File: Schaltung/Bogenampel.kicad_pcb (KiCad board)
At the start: 2 copper layers, 95 x 62 mm, 32 parts, among them J1 WS2812B Stripe Timer, J10 Display, J2 Conn_01x04_Pin, J3 DC/DC Boost, J4 Jumper: 5V/Ext Voltage, J5 Buzzer, J6 Battery, J7 Input 4, J8 Input 5, J9 Power Bank, Q1 IRLZ44N, U1 NRF24L01_Breakout, U2 TXS0108EPW

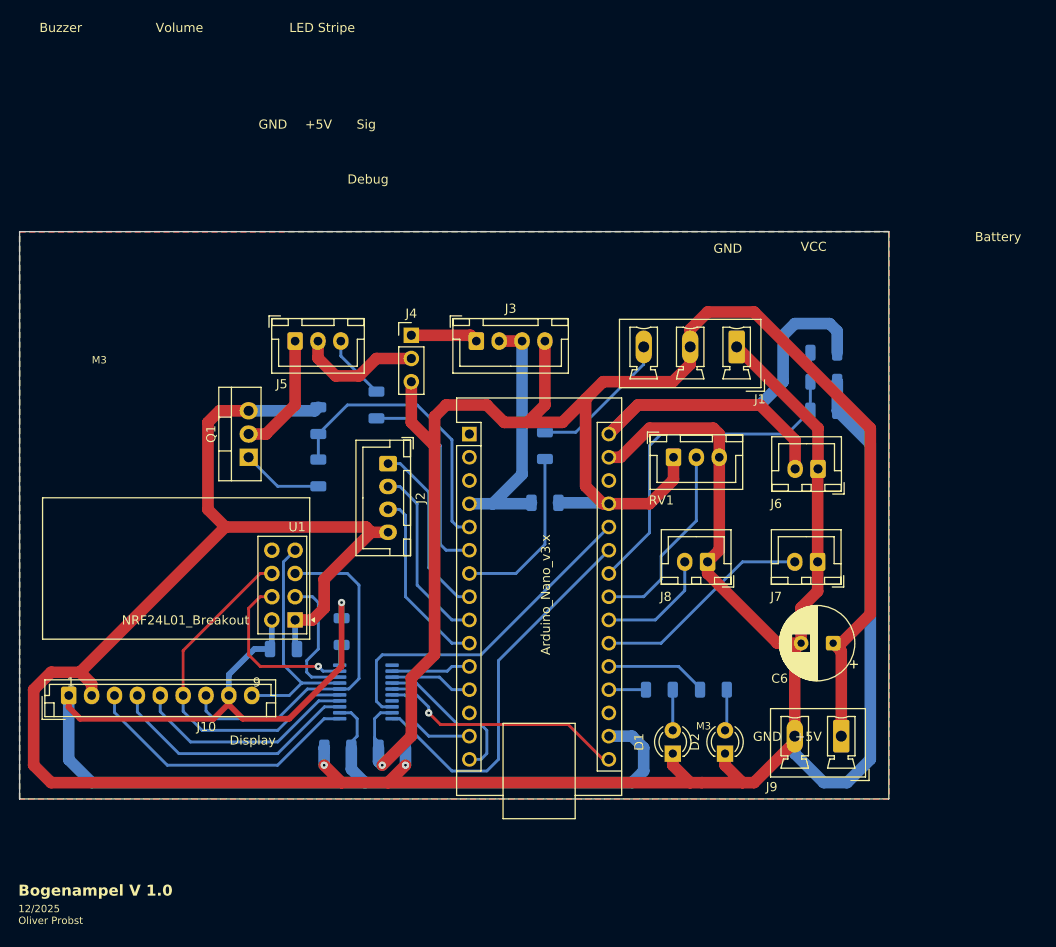
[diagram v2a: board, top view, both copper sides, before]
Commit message: 7-Segment LED-Display und Gruppen-Anzeige implementiert
Empfänger:
- 158 LEDs konfiguriert: 16 Gruppe A/B, 16 Gruppe C/D, 126 für 3×7-Segment Displays
- Timer-Countdown auf 7-Segment-Display (Grün > Orange > Rot)
- Vorbereitungsphase (10s) mit Countdown in ROT
- Orange statt Gelb für letzte 30 Sekunden (besserer Kontrast zu Grün)
- Gruppen-Farbe synchron mit Display-Farbe
- Gruppen-Umschaltung korrigiert (inaktive Gruppe wird ausgeschaltet)
- Buzzer-Funktionen verbessert (explizites Pin-Reset)
- segmentMap korrigiert für korrekte 7-Segment-Darstellung
- Display-Reihenfolge angepasst (1er, 10er, 100er von links nach rechts)

Sender:
- Gruppen-Kommandos jetzt zur richtigen Zeit gesendet (nach advanceToNextGroup)

🤖 Generated with Claude Code

Co-Authored-By: Claude Sonnet 4.5 <noreply@anthropic.com>
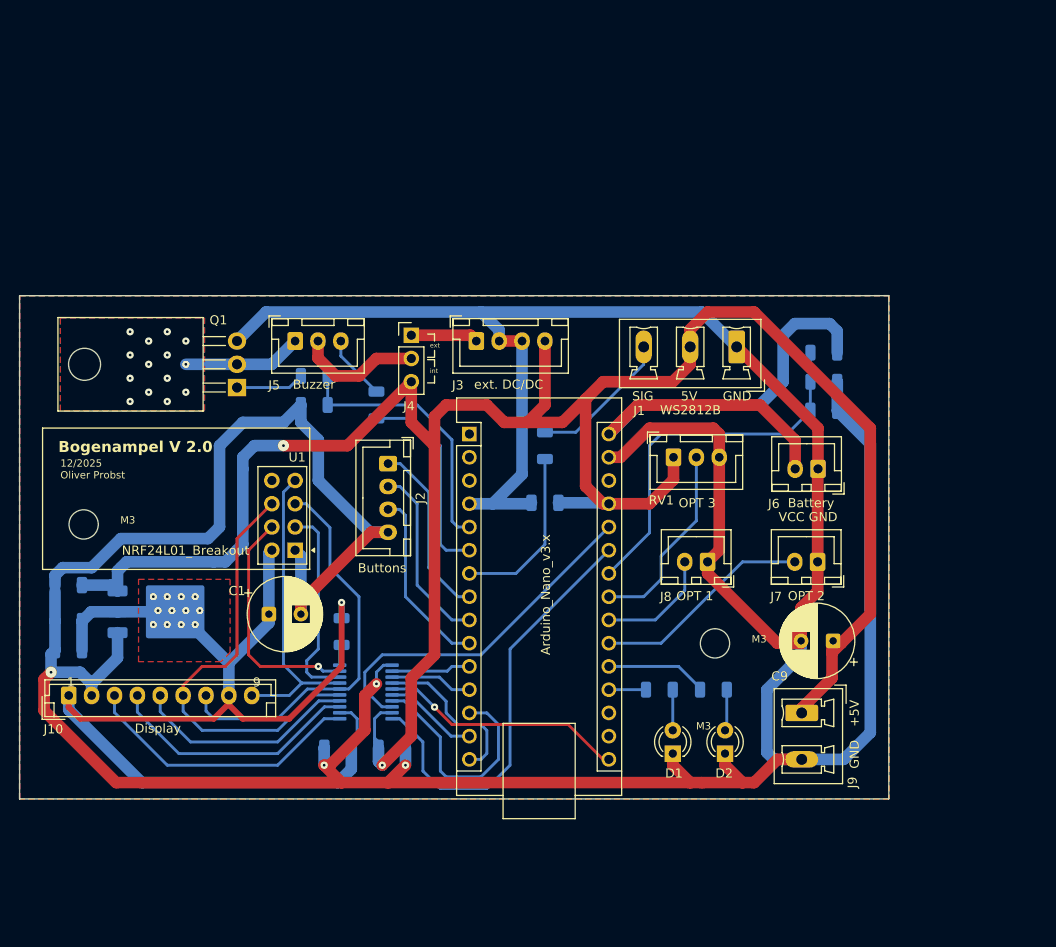
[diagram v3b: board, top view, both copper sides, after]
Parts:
- added C5: 100nF, Capacitor_SMD:C_1206_3216Metric, B.Cu at (93.3, 94.7)
- added C7: 10µF, Capacitor_SMD:C_1206_3216Metric, B.Cu at (93.3, 91.6)
- added C8: 10µF, Capacitor_SMD:C_1206_3216Metric, B.Cu at (93.3, 87.6)
- added REF**: MountingHole_3.2mm_M3, MountingHole:MountingHole_3.2mm_M3, F.Cu at (95.0, 81.0)
- added REF**: MountingHole_3.2mm_M3, MountingHole:MountingHole_3.2mm_M3, F.Cu at (164.0, 94.0)
- added U3: LM1117DT-3.3, Package_TO_SOT_SMD:TO-252-3_TabPin2, B.Cu at (103.7, 90.5)
- C1: value 10µF -> 100µF; footprint Capacitor_SMD:C_1206_3216Metric -> Capacitor_THT:CP_Radial_D8.0mm_P3.50mm; moved to F.Cu
- Q1: footprint Package_TO_SOT_THT:TO-220-3_Vertical -> Package_TO_SOT_THT:TO-220-3_Horizontal_TabDown
- moved R3 10.6 mm to (120.2, 64.8), turned to 180 degrees
- moved Q1 7.73 mm to (111.8, 66.0)
- moved U1 7.62 mm to (118.1, 83.8)
- moved J9 5.01 mm to (173.5, 101.6), turned to -90 degrees
- moved C1 4.13 mm to (115.2, 90.8)
- moved R4 1.77 mm to (120.2, 67.9), turned to 0 degrees
- moved C9 0.25 mm to (176.9, 93.7)
- renumbered C5 to C6, C6 to C9
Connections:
- A1 pad 17: +3.3V -> unconnected-(A1-3V3-Pad17)
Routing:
- net GND: track 377.4 -> 464.4 mm, vias 2 -> 4
- net +5V: track 193.1 -> 245.6 mm, vias 1 -> 2
- net /DSPL_DC_5V: track 0.00 -> 25.5 mm
- net +3.3V: track 145.5 -> 130.0 mm, vias 1 -> 13
- net /SPI_3V3.MOSI: track 39.4 -> 47.8 mm
- net /NRF_CS_3V3: track 14.8 -> 22.4 mm
- net /SPI_3V3.MISO: track 26.0 -> 33.7 mm
- net /NRF_CSN_3V3: track 18.8 -> 25.7 mm
- net /SPI_3V3.SCK: track 38.3 -> 43.3 mm
- net /DSPL_CS_5V: track 42.4 -> 46.9 mm
- net Net-(A1-D2): track 31.3 -> 29.4 mm
- net Net-(Q1-G): track 8.94 -> 7.51 mm
- net /SPI_5V.MOSI: track 11.4 -> 10.3 mm
- net /DSPL_RES_5V: track 37.9 -> 38.9 mm
- net /SPI_5V.MISO: track 17.2 -> 17.9 mm
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- added copper zone on F.Cu, net +3.3V
- added copper zone on B.Cu, net Net-(J5-Pin_1)
- added copper zone on F.Cu, net Net-(J5-Pin_1)
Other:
- board size 95 x 62 mm -> 95 x 55 mm
- board text added: "5V"
- board text added: "Bogenampel V 2.0"
- board text added: "Buttons"
- board text added: "OPT 1"
- board text added: "OPT 2"
- board text added: "OPT 3"
- board text added: "SIG"
- board text added: "WS2812B"
- board text added: "ext"
- board text added: "ext. DC/DC"
- board text added: "int"
- board text removed: "Bogenampel V 1.0"
- board text removed: "Debug"
- board text removed: "LED Stripe"
- board text removed: "Sig"
- board text removed: "Volume"

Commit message: DEBUG_SHORT_TIMES aktiviert mit optimierten Zeiten
Software-Änderungen:
- DEBUG_SHORT_TIMES auf 1 gesetzt (aktiviert)
- Vorbereitungsphase: 5 Sekunden (unverändert)
- Schießzeit: 15 Sekunden für beide Modi (statt 6s/12s)
- Gelbe Ampel: Aktivierung in den letzten 5 Sekunden (statt 30s)
- Empfänger Serial Baud: 115200 statt 57600
- CMD_STOP Handler vereinfacht (nur Vorbereitung zurücksetzen)

Schaltungs-Änderungen:
- MOSFET Q1 Footprint: TO-220-3_Vertical statt Horizontal
- 100nF SMD-Entkopplungskondensator (C10) hinzugefügt
- Spannungsversorgung verbessert

🤖 Generated with [Claude Code](https://claude.com/claude-code)

Co-Authored-By: Claude Sonnet 4.5 <noreply@anthropic.com>
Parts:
- added C10: 100nF, Capacitor_SMD:C_1206_3216Metric, B.Cu at (116.9, 87.4)
- Q1: footprint Package_TO_SOT_THT:TO-220-3_Horizontal_TabDown -> Package_TO_SOT_THT:TO-220-3_Vertical

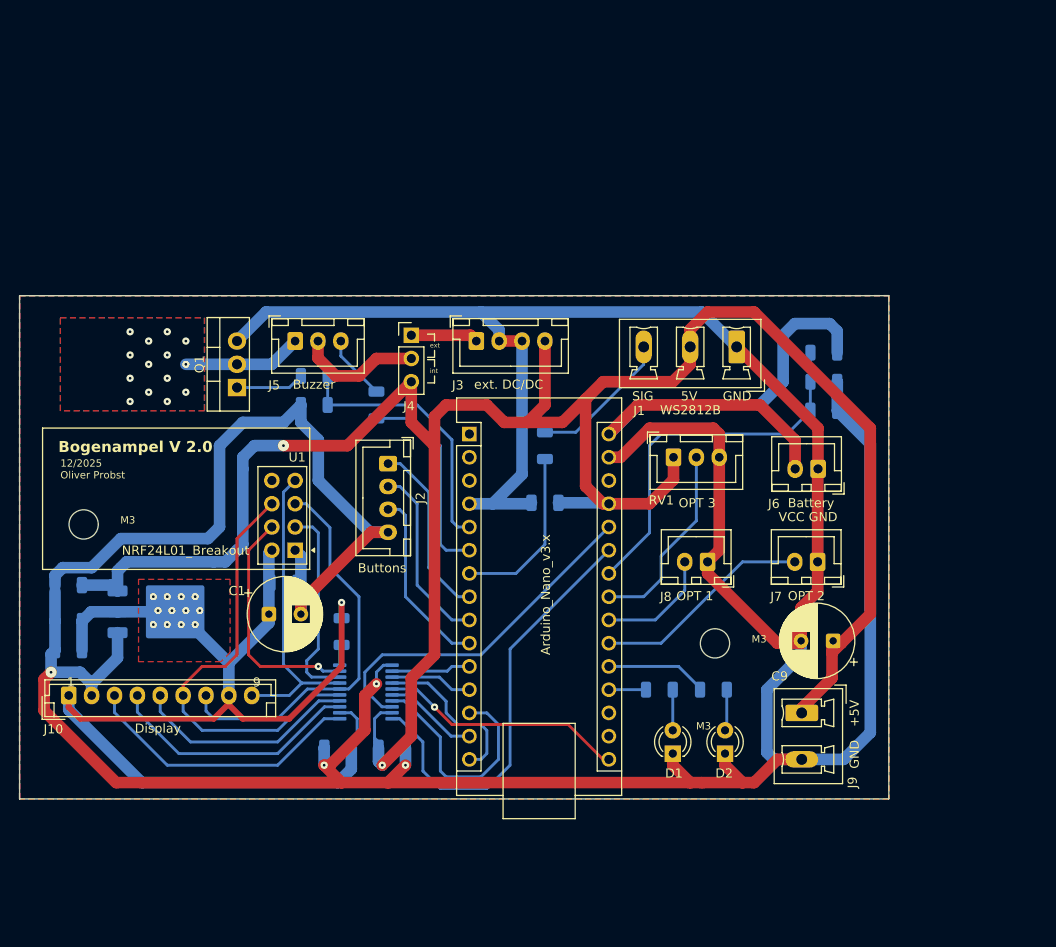
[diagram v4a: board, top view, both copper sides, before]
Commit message: Dokumentation aktualisiert und Schaltung Version 2.2
- HARDWARE.md: Pin-Belegungen korrigiert (NRF D9/D8, Buttons D5/D6/D7, Voltage A5, Buzzer D4)
- README.md: Features, Pin-Tabellen und Kommunikation aktualisiert (158 LEDs, 11 Kommandos)
- Sender/README.md: Alle Features als implementiert markiert, State Machine erweitert
- Sender/SETUP.md: Test-Sektion aktualisiert
- CLAUDE.md: Komplett überarbeitet mit aktuellem Projekt-Stand
- Schaltung: Version 2.2 - bereit für Fertigung
- Test-Dateien entfernt (TestEmpfaenger, TestSender)

🤖 Generated with [Claude Code](https://claude.com/claude-code)

Co-Authored-By: Claude Sonnet 4.5 <noreply@anthropic.com>
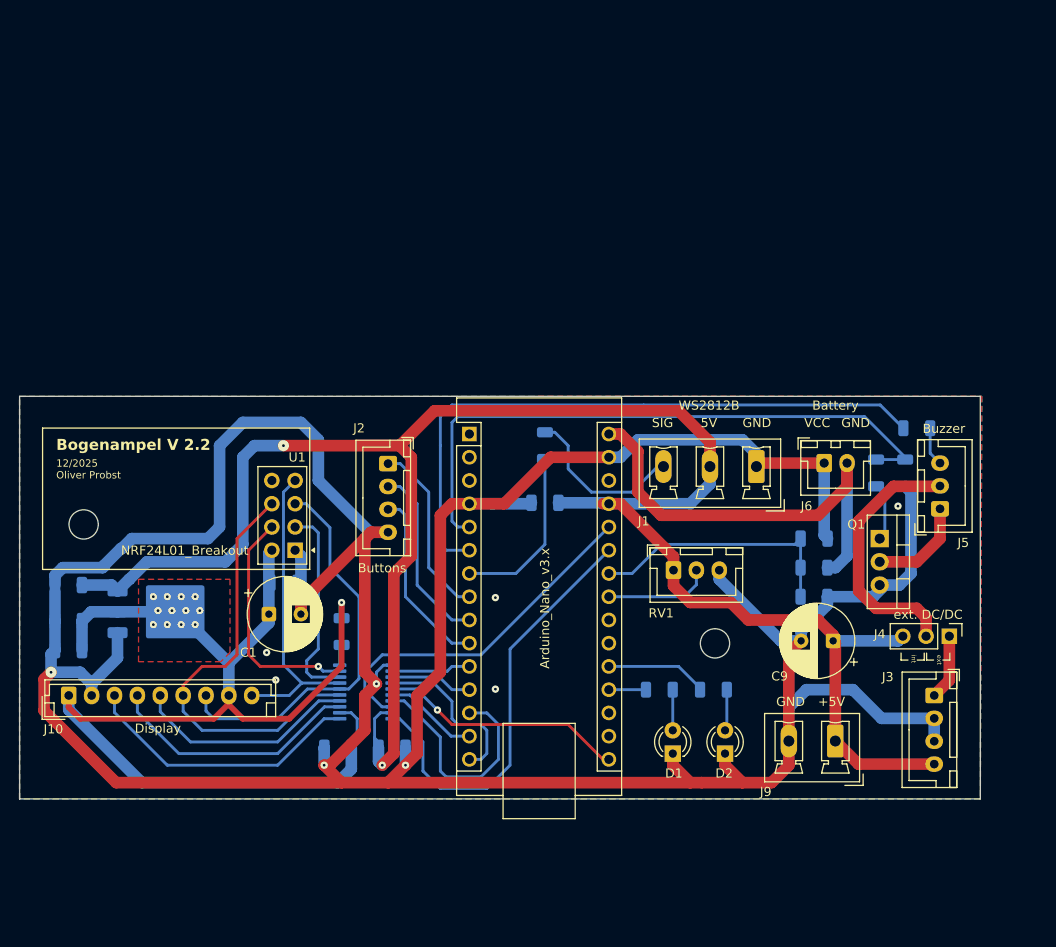
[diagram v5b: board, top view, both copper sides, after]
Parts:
- removed J7: Input 4, Connector_JST:JST_XH_B2B-XH-A_1x02_P2.50mm_Vertical
- removed J8: Input 5, Connector_JST:JST_XH_B2B-XH-A_1x02_P2.50mm_Vertical
- moved J5 72.8 mm to (188.6, 79.3), turned to 90 degrees
- moved Q1 72.2 mm to (182.0, 82.5), turned to -90 degrees
- moved J4 67.4 mm to (189.6, 93.2), turned to -90 degrees
- moved R4 65.0 mm to (184.8, 75.4), turned to 90 degrees
- moved J3 63.3 mm to (188.0, 99.7), turned to -90 degrees
- moved R3 62.3 mm to (181.6, 75.4), turned to -90 degrees
- moved R2 59.1 mm to (186.1, 70.5), turned to 0 degrees
- moved R8 23.5 mm to (174.8, 88.9)
- moved R7 23.5 mm to (174.8, 85.7)
- moved C3 14.0 mm to (174.8, 82.5)
- moved J1 13.3 mm to (168.5, 74.7)
- moved RV1 12.3 mm to (159.5, 86.0)
- moved J9 4.79 mm to (177.2, 104.7), turned to 180 degrees
- moved J6 0.93 mm to (175.9, 74.3), turned to 0 degrees
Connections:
- A1 pad 21: /DI4 -> unconnected-(A1-A2-Pad21)
- A1 pad 22: /DI5 -> unconnected-(A1-A3-Pad22)
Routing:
- net GND: track 464.4 -> 408.5 mm, vias 4 -> 9
- net Net-(A1-D3): track 22.5 -> 69.6 mm
- net Net-(A1-D2): track 29.4 -> 68.0 mm
- net +5V: track 245.6 -> 215.4 mm
- net /DI4: track 24.0 -> 0.00 mm
- net Net-(J4-Pin_2): track 13.7 -> 28.8 mm
- net +BATT: track 62.0 -> 49.0 mm
- net /DI5: track 12.8 -> 0.00 mm
- net /BAT_MON: track 41.3 -> 28.9 mm
- net /AI1: track 21.4 -> 11.7 mm
- net Net-(J5-Pin_3): track 7.13 -> 4.26 mm
- net Net-(J5-Pin_1): track 13.0 -> 10.2 mm, vias 14 -> 0
- net Net-(J1-Pin_3): track 15.8 -> 18.3 mm
- net Net-(Q1-G): track 7.51 -> 6.11 mm
- removed copper zone on B.Cu, net (none)
- removed copper zone on F.Cu, net (none)
- removed copper zone on B.Cu, net Net-(J5-Pin_1)
- removed copper zone on F.Cu, net Net-(J5-Pin_1)
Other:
- board size 95 x 55 mm -> 105 x 44 mm
- board text added: "Bogenampel V 2.2"
- board text removed: "1"
- board text removed: "9"
- board text removed: "Bogenampel V 2.0"
- board text removed: "M3"
- board text removed: "OPT 1"
- board text removed: "OPT 2"
- board text removed: "OPT 3"

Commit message: Bug: A6 & A7 durch A2 & A3 ersetzt für Digital Output
Co-Authored-By: Claude Opus 4.5 <noreply@anthropic.com>
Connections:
- A1 pad 21: unconnected-(A1-A2-Pad21) -> /DSPL_CS_5V
- A1 pad 22: unconnected-(A1-A3-Pad22) -> /DSPL_RES_5V
- A1 pad 25: /DSPL_CS_5V -> unconnected-(A1-A6-Pad25)
- A1 pad 26: /DSPL_RES_5V -> unconnected-(A1-A7-Pad26)
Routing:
- net /DSPL_CS_5V: track 46.9 -> 38.7 mm
- net /DSPL_RES_5V: track 38.9 -> 34.7 mm
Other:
- board text added: "01/2026 Oliver Probst"
- board text added: "Bogenampel V 2.3"
- board text removed: "12/2025 Oliver Probst"
- board text removed: "Bogenampel V 2.2"
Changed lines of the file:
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@@
 	(net 45 "Net-(J5-Pin_1)")
 	(net 46 "unconnected-(A1-3V3-Pad17)")
-	(net 47 "unconnected-(A1-A2-Pad21)")
-	(net 48 "unconnected-(A1-A3-Pad22)")
+	(net 47 "unconnected-(A1-A7-Pad26)")
+	(net 48 "unconnected-(A1-A6-Pad25)")
 	(footprint "LED_THT:LED_D3.0mm"
 		(layer "F.Cu")
@@
 			(layers "*.Cu" "*.Mask")
 			(remove_unused_layers no)
-			(net 47 "unconnected-(A1-A2-Pad21)")
+			(net 21 "/DSPL_CS_5V")
 			(pinfunction "A2")
 			(pintype "bidirectional")
@@
 			(layers "*.Cu" "*.Mask")
 			(remove_unused_layers no)
-			(net 48 "unconnected-(A1-A3-Pad22)")
+			(net 6 "/DSPL_RES_5V")
 			(pinfunction "A3")
 			(pintype "bidirectional")
@@
 			(layers "*.Cu" "*.Mask")
 			(remove_unused_layers no)
-			(net 21 "/DSPL_CS_5V")
+			(net 48 "unconnected-(A1-A6-Pad25)")
 			(pinfunction "A6")
 			(pintype "bidirectional")
@@
 			(layers "*.Cu" "*.Mask")
 			(remove_unused_layers no)
-			(net 6 "/DSPL_RES_5V")
+			(net 47 "unconnected-(A1-A7-Pad26)")
 			(pinfunction "A7")
 			(pintype "bidirectional")
@@
 			)
 		)
-		(property "Datasheet" ""
+		(property "Datasheet" "http://www.irf.com/product-info/datasheets/data/irlz44n.pdf"
 			(at 0 0 90)
 			(layer "F.Fab")
@@
 			)
 		)
-		(property "Description" ""
+		(property "Description" "47A Id, 55V Vds, 22mOhm Rds Single N-Channel HEXFET Power MOSFET, TO-220AB"
 			(at 0 0 90)
 			(layer "F.Fab")
@@
 		)
 	)
-	(gr_text "Bogenampel V 2.2"
+	(gr_text "Bogenampel V 2.3"
 		(at 92 73 0)
 		(layer "F.SilkS")
@@
 		)
 	)
-	(gr_text "12/2025\nOliver Probst"
+	(gr_text "01/2026\nOliver Probst"
 		(at 92 76.073 0)
 		(layer "F.SilkS")
@@
 		)
 	)
-	(gr_text "12/2025\nOliver Probst"
+	(gr_text "01/2026\nOliver Probst"
 		(at 109 76.073 0)
 		(layer "B.SilkS")
@@
 		)
 	)
-	(gr_text "Bogenampel V 2.2"
-		(at 109 73.025 0)
+	(gr_text "Bogenampel V 2.3"
+		(at 109 73 0)
 		(layer "B.SilkS")
 		(effects
@@
 	)
 	(segment
+		(start 143.75 95.25)
+		(end 147.56 91.44)
+		(width 0.318)
+		(layer "B.Cu")
+		(net 6)
+	)
+	(segment
 		(start 125.73 97.155)
 		(end 127.635 95.25)
@@
 	)
 	(segment
+		(start 147.56 91.44)
+		(end 152.4 91.44)
+		(width 0.318)
+		(layer "B.Cu")
+		(net 6)
+	)
+	(segment
+		(start 138.43 95.25)
+		(end 143.75 95.25)
+		(width 0.318)
+		(layer "B.Cu")
+		(net 6)
+	)
+	(segment
 		(start 128.71 100.935)
 		(end 127.605 100.935)
@@
 	)
 	(segment
-		(start 138.43 95.25)
-		(end 152.4 81.28)
-		(width 0.3175)
-		(layer "B.Cu")
-		(net 6)
-	)
-	(segment
 		(start 151.765 106.68)
 		(end 152.4 106.68)
@@
 	)
 	(segment
-		(start 152.4 83.82)
-		(end 141.605 94.615)
+		(start 132.08 107.95)
+		(end 133.985 109.855)
+		(width 0.3175)
+		(layer "B.Cu")
+		(net 21)
+	)
+	(segment
+		(start 141.605 101.395)
+		(end 141.605 107.315)
 		(width 0.318)
 		(layer "B.Cu")
@@
 	)
 	(segment
-		(start 132.08 107.95)
-		(end 133.985 109.855)
-		(width 0.3175)
+		(start 149.02 93.98)
+		(end 141.605 101.395)
+		(width 0.318)
 		(layer "B.Cu")
 		(net 21)
 	)
 	(segment
-		(start 141.605 94.615)
-		(end 141.605 107.315)
+		(start 152.4 93.98)
+		(end 149.02 93.98)
 		(width 0.318)
 		(layer "B.Cu")
